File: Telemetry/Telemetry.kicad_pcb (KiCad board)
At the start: 2 copper layers, 54 parts, among them J5 Conn_02x05_Odd_Even, Q3 Q_NMOS_GSD, SW1 SW_Push, SW3 SW_Push, U3 MAX485E, U4 STM32F103C8Tx, U5 LD1117S50TR_SOT223, U6 MCP1700-3302E_SOT23

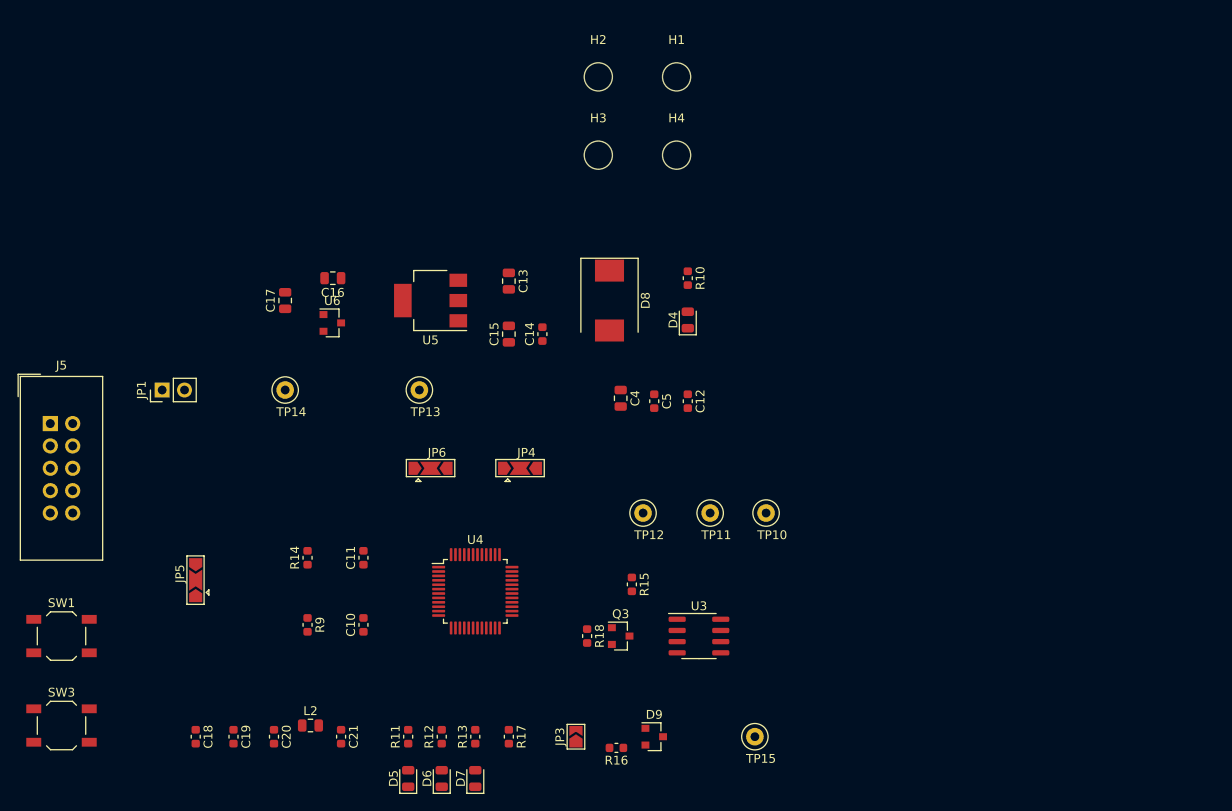
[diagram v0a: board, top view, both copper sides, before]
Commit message: Telemetry/: Create a pcd layout
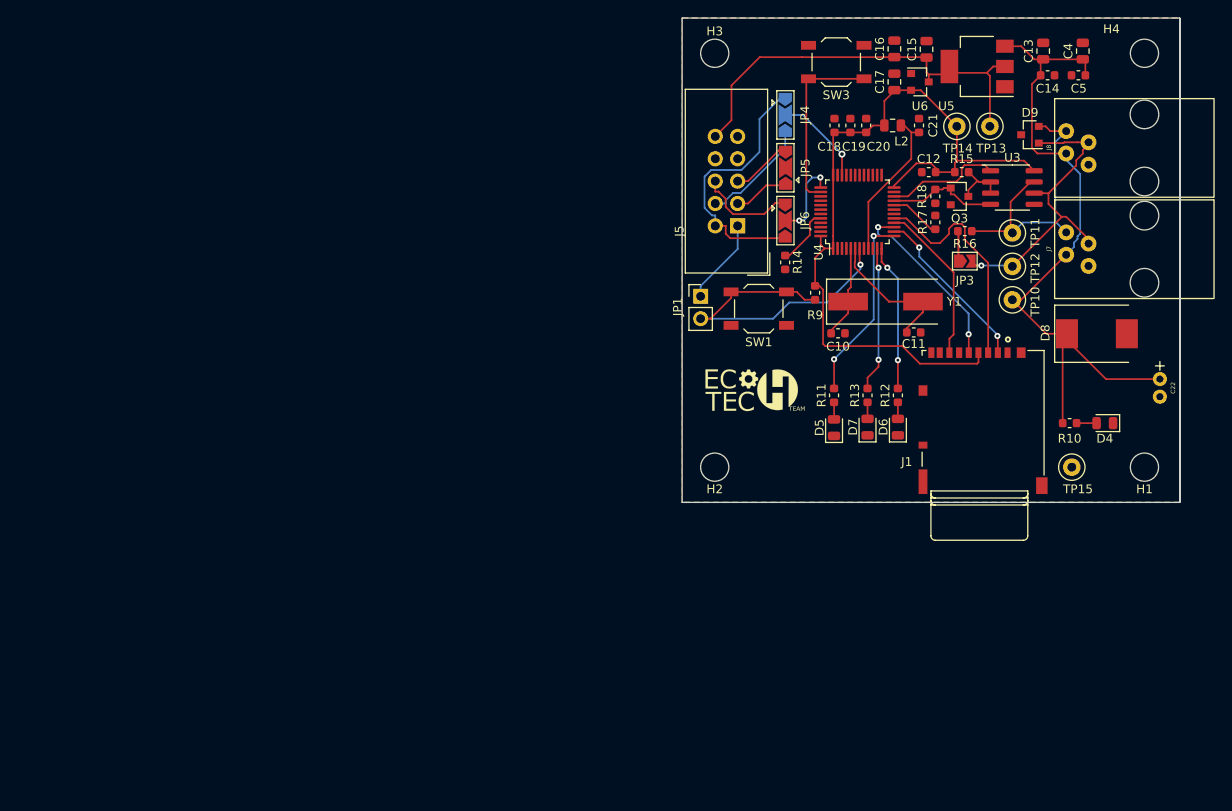
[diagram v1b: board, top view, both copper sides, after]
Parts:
- added C22: 100u, Footprints:C_Radial_D5.0mm_H11.0mm_P2.00mm, F.Cu at (157.8, 141.0)
- added G1: EchoTech Team, Footprints:EcoTech, F.Cu at (111.5, 142.5)
- added J1: Micro_SD_Card, Footprints:DM3AT-microSD, F.Cu at (137.2, 138.0)
- added J7: 4P4C, Footprints:4P4C, F.Cu at (156.0, 126.2)
- added J8: 4P4C, Footprints:4P4C, F.Cu at (156.0, 114.8)
- added Y1: 8Mhz, Footprints:Crystal_SMD_HC49-SD, F.Cu at (126.6, 132.2)
- moved SW3 115.8 mm to (121.0, 105.0), turned to 180 degrees
- moved C18 100.4 mm to (120.8, 112.2), turned to 90 degrees
- moved C19 98.6 mm to (122.6, 112.2), turned to 90 degrees
- moved C20 96.6 mm to (124.4, 112.2), turned to 90 degrees
- moved C21 95.5 mm to (130.4, 112.2), turned to 90 degrees
- moved L2 94.9 mm to (127.4, 112.2)
- moved SW1 87.5 mm to (112.2, 133.0), turned to 180 degrees
- moved TP14 81.9 mm to (134.7, 112.3)
- moved JP5 81.7 mm to (115.2, 117.0)
- moved J5 81.2 mm to (109.8, 123.6), turned to 180 degrees
- moved D9 80.6 mm to (143.0, 113.2), turned to 180 degrees
- moved R17 75.9 mm to (132.2, 123.2), turned to 90 degrees
- moved C17 73.5 mm to (127.6, 107.2)
- moved U6 72.1 mm to (130.5, 107.2)
- moved TP13 71.4 mm to (138.4, 112.3)
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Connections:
- JP4 pad : (no net) -> /4
- JP5 pad : (no net) -> Net-(J5-Pad5)
- JP6 pad : (no net) -> /2
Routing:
- net +3V3: track 0.00 -> 90.2 mm
- net +12V: track 0.00 -> 79.1 mm
- net +5V: track 0.00 -> 48.9 mm
- net /RST: track 0.00 -> 37.9 mm, vias 0 -> 1
- net /A: track 0.00 -> 36.7 mm, vias 0 -> 1
- net /B: track 0.00 -> 32.9 mm
- net /2: track 0.00 -> 30.4 mm
- net /MOSI: track 0.00 -> 26.0 mm
- net /LED1: track 0.00 -> 21.5 mm, vias 0 -> 2
- net /SCK: track 0.00 -> 21.0 mm, vias 0 -> 2
- net Net-(SW3-Pad1): track 0.00 -> 20.7 mm
- net /CS: track 0.00 -> 19.3 mm, vias 0 -> 2
- net /MISO: track 0.00 -> 18.4 mm
- net +3.3VA: track 0.00 -> 17.6 mm
- net /LED3: track 0.00 -> 16.9 mm, vias 0 -> 2
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- added copper zone on B.Cu, net GND
- added copper zone on F.Cu, net GND
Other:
- board outline added: 56.5 x 55 mm
- net class Default: trace_width 0.25 -> 0.2; via_dia 0.8 -> 0.7; via_drill 0.4 -> 0.3
- net class Signal added: clearance 0.2, trace_width 0.2, via_dia 0.7, via_drill 0.3

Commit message: create version 1.0.1
Signed-off-by: Cezary Sobczak <cezary.sobczak@3mdeb.com>
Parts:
- moved SW3 36.6 mm to (112.2, 140.5), turned to 0 degrees
- moved C18 13.1 mm to (119.2, 125.2), turned to 180 degrees
- moved C4 11.6 mm to (143.5, 114.0), turned to 270 degrees
- moved C22 11.0 mm to (146.8, 141.0)
- moved C15 8.51 mm to (122.8, 103.0)
- moved C16 8.51 mm to (119.1, 103.0)
- moved C17 8.51 mm to (119.1, 106.8)
- moved U5 8.51 mm to (128.5, 105.0)
- moved U6 8.51 mm to (122.0, 106.8)
- moved D5 8.03 mm to (127.9, 142.9)
- moved R11 8.03 mm to (127.9, 139.2)
- moved G1 7.46 mm to (116.2, 148.2)
- moved D9 7.42 mm to (147.3, 107.2), turned to 270 degrees
- moved C13 7.25 mm to (137.2, 103.5)
- moved C14 7.25 mm to (137.8, 106.2), turned to 180 degrees
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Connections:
- JP4 pad : /4 -> (no net)
- JP5 pad : Net-(J5-Pad5) -> (no net)
- JP6 pad : /2 -> (no net)
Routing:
- net +3V3: track 90.2 -> 121.0 mm, vias 0 -> 1
- net Net-(SW3-Pad1): track 20.7 -> 51.3 mm
- net +5V: track 48.9 -> 40.5 mm
- net /A: track 36.7 -> 44.3 mm
- net /B: track 32.9 -> 40.4 mm, vias 0 -> 1
- net Net-(Q3-Pad3): track 6.40 -> 11.7 mm
- net Net-(C11-Pad1): track 15.8 -> 20.6 mm, vias 0 -> 2
- net /LED1: track 21.5 -> 16.7 mm
- net +12V: track 79.1 -> 74.5 mm
- net /RX: track 13.3 -> 17.5 mm, vias 0 -> 2
- net /SCK: track 21.0 -> 24.7 mm, vias 2 -> 0
- net +3.3VA: track 17.6 -> 15.1 mm
- net /RST: track 37.9 -> 35.7 mm, vias 1 -> 2
- net /2: track 30.4 -> 28.3 mm
- net /LED2: track 16.7 -> 14.8 mm
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
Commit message: Telemetry/: add rev v1.0
Signed-off-by: Cezarus27 <cs.pol234@gmail.com>
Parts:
- moved TP15 41.6 mm to (137.8, 110.6)
- moved C12 0.82 mm to (132.3, 117.2), turned to 90 degrees
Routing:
- net /6: track 11.1 -> 14.3 mm
- net /2: track 28.3 -> 29.8 mm
- net Net-(SW3-Pad1): track 51.3 -> 51.9 mm
- net +3V3: track 121.0 -> 121.5 mm, vias 1 -> 2
- net GND: vias 64 -> 85
- net (no net): vias 0 -> 2
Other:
- board text added: "Telemetry v1.0 26.03.2020"
